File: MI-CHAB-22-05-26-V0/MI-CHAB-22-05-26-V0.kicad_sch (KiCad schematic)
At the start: 17 parts, among them J1 Beaglebone-green-P9, J2 Beaglebone-green-P8, J3 Conn_02x06_Odd_Even, J4 Conn_02x06_Odd_Even, J5 Conn_02x06_Odd_Even, Q1 IRLML6244

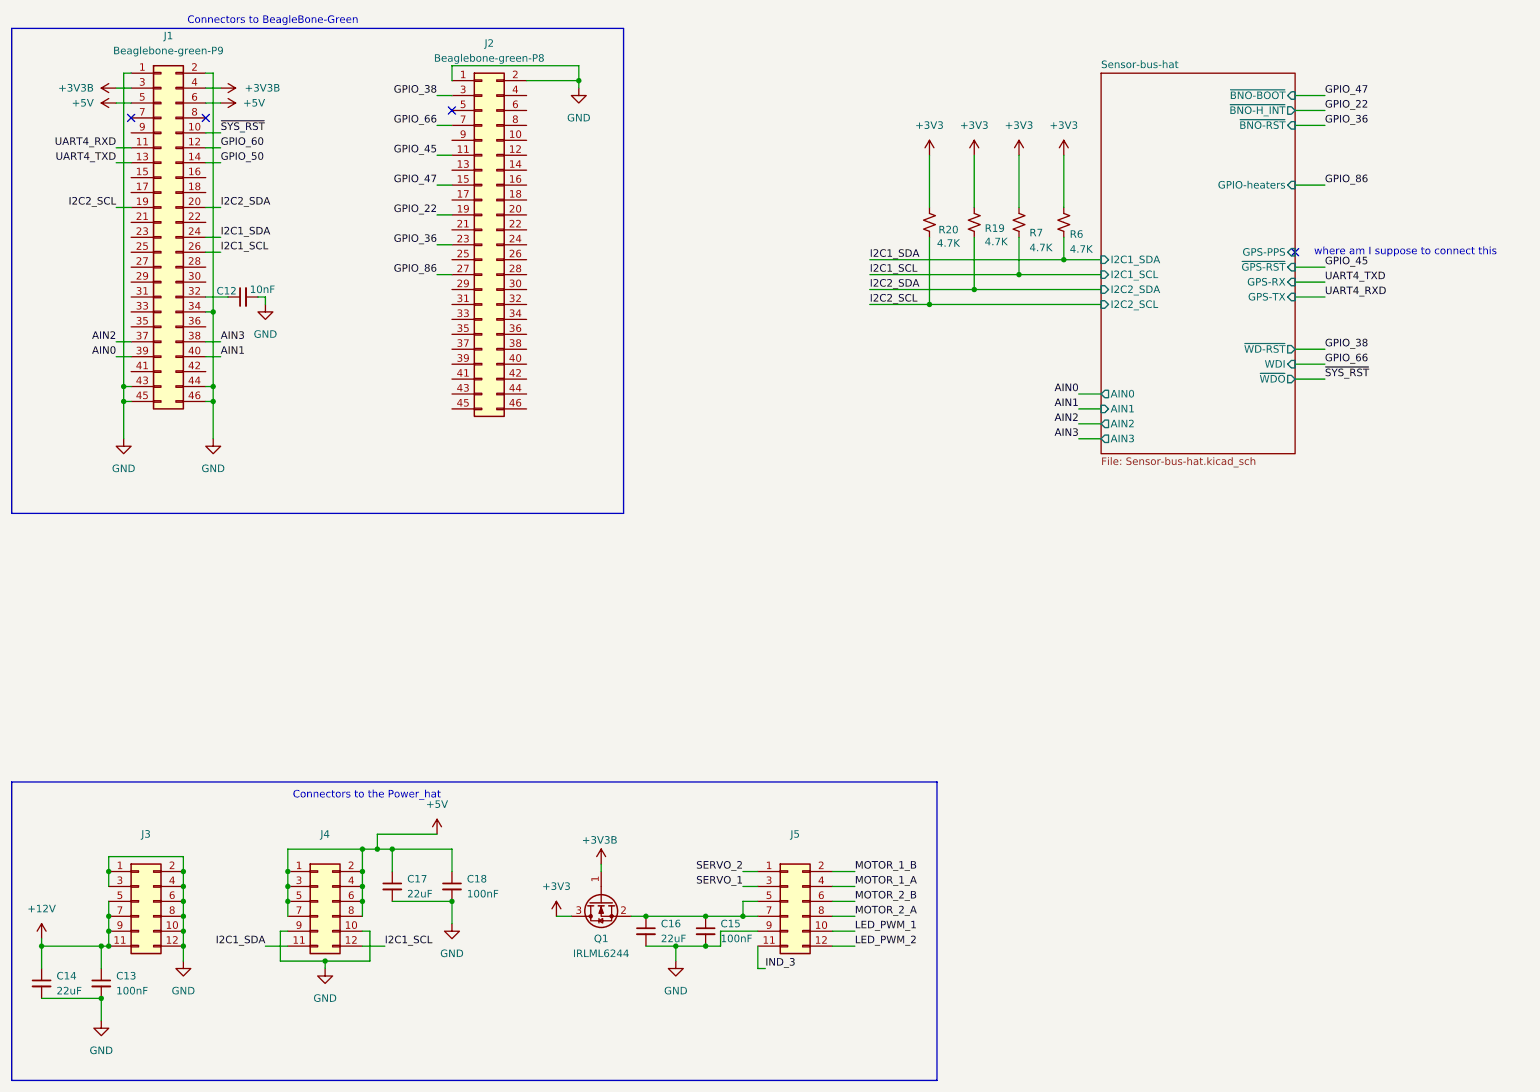
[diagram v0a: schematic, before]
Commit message: revision 0.1 - added debug stuff, CAN interface, I2C buffer
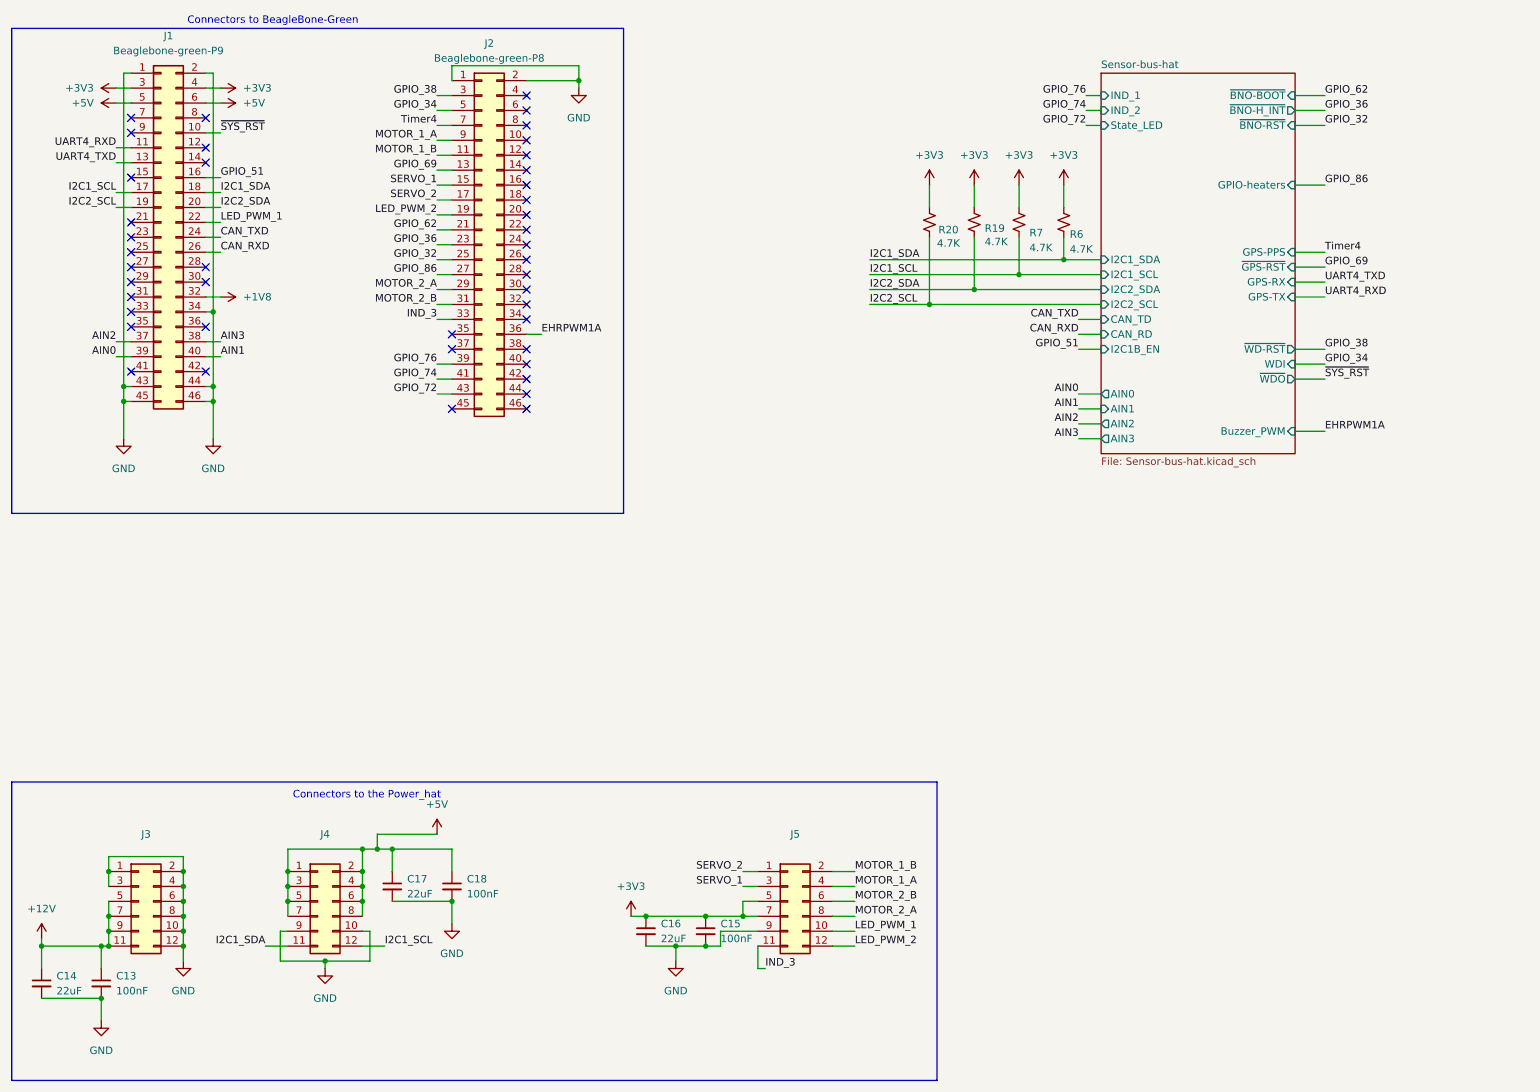
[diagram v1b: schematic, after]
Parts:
- removed C12: 10nF, symbol Device:C_Small
- removed Q1: IRLML6244, Package_TO_SOT_SMD:SOT-23, symbol Transistor_FET:IRLML6244
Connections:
- net GPIO_22 is gone; now on net LED_PWM_2: J2.19 (Pin_19)
- net GPIO_45 is gone; now on net MOTOR_1_B: J2.11 (Pin_11)
- net GPIO_47 is gone; now on net SERVO_1: J2.15 (Pin_15)
- net +3V3: now also C15.1, C16.1, J1.3 (Pin_3), J1.4 (Pin_4), J5.5 (Pin_5), J5.7 (Pin_7)
- net I2C1_SCL: now also J1.17 (Pin_17); no longer J1.26 (Pin_26)
- net I2C1_SDA: now also J1.18 (Pin_18); no longer J1.24 (Pin_24)
- net IND_3: now also J2.33 (Pin_33)
- net LED_PWM_1: now also J1.22 (Pin_22)
- net MOTOR_1_A: now also J2.9 (Pin_9)
- net MOTOR_2_A: now also J2.29 (Pin_29)
- net MOTOR_2_B: now also J2.31 (Pin_31)
- net SERVO_2: now also J2.17 (Pin_17)
- net +1V8: now reaches J1.32 (Pin_32)
- net GPIO_69: now reaches J2.13 (Pin_13)
- net GPIO_62: now reaches J2.21 (Pin_21)
- net GPIO_32: now reaches J2.25 (Pin_25)
- net EHRPWM1A: now reaches J2.36 (Pin_36)
- net GPIO_76: now reaches J2.39 (Pin_39)
- net GPIO_74: now reaches J2.41 (Pin_41)
- net GPIO_72: now reaches J2.43 (Pin_43)
- net GPIO_34: now reaches J2.5 (Pin_5)
- net GPIO_51: now reaches J1.16 (Pin_16)
- net GPIO_50: no longer names the net of J1.14 (Pin_14)
- net GPIO_60: no longer names the net of J1.12 (Pin_12)
- net GPIO_66 renamed Timer4
- new net CAN_RXD: J1.26 (Pin_26)
- new net CAN_TXD: J1.24 (Pin_24)
- no-connect marks 4 -> 43
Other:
- sheet Sensor-bus-hat ports: added Buzzer_PWM, CAN_RD, CAN_TD, I2C1B_EN, IND_1, IND_2, State_LED; removed none
- note removed: "where am I suppose to connect this"
